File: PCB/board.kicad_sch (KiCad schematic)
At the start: 171 parts, among them J1 Micro_SD_Card, J10 Conn_01x10, J11 Conn_01x02, J12 Conn_02x04_Odd_Even, J13 Conn_01x02, J14 Conn_01x02, J15 Conn_01x03, J16 Conn_01x02, J17 Conn_01x05, J18 Conn_01x04, J19 Conn_01x04, J2 Conn_ARM_JTAG_SWD_10, J20 Conn_01x02, J21 Conn_01x03, J22 Conn_02x04_Odd_Even, J23 Conn_01x04, J24 Conn_01x04, J25 Conn_01x02, J26 Conn_01x03, J27 Conn_02x04_Odd_Even, J28 Conn_01x04, J29 Conn_01x04, J30 Conn_01x02, J31 Conn_01x03, J32 Conn_01x02, J33 Conn_01x02, J34 Conn_01x02, J35 Conn_01x02, J36 Conn_01x02, J37 Conn_01x02, J4 Conn_01x04, J5 Conn_01x04, J6 Conn_01x02, J7 Conn_01x03, J8 Conn_02x04_Odd_Even, J9 Conn_01x10, P1 USB_C_Plug_USB2.0, Q1 IRLML6402, Q2 NMOS, Q3 NMOS, Q4 NMOS, Q5 NMOS, Q6 NMOS, SW1 SW_SPST, SW2 SW_Push, U1 STM32H743VITx, U2 AMS1117-3.3, U3 TPS54331, U4 TMC2209_SILENTSTEPSTICK, U5 TMC2209_SILENTSTEPSTICK, U6 TMC2209_SILENTSTEPSTICK, U7 TMC2209_SILENTSTEPSTICK, Y1 25 MHz

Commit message: added footprints to the PSU
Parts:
- C17: footprint (none) -> Capacitor_THT:CP_Radial_D6.3mm_P2.50mm
- D2: footprint (none) -> Package_TO_SOT_THT:TO-220-2_Horizontal_TabDown
- F1: footprint (none) -> Fuse:Fuse_1812_4532Metric
- J37: footprint (none) -> TerminalBlock_Phoenix:TerminalBlock_Phoenix_MKDS-1,5-2-5.08_1x02_P5.08mm_Horizontal
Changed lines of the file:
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@@
 			)
 		)
-		(property "Footprint" ""
+		(property "Footprint" "Capacitor_THT:CP_Radial_D6.3mm_P2.50mm"
 			(at 83.5152 31.75 0)
 			(effects
@@
 			)
 		)
-		(property "Footprint" ""
+		(property "Footprint" "TerminalBlock_Phoenix:TerminalBlock_Phoenix_MKDS-1,5-2-5.08_1x02_P5.08mm_Horizontal"
 			(at 69.85 26.67 0)
 			(effects
@@
 			)
 		)
-		(property "Footprint" ""
+		(property "Footprint" "Package_TO_SOT_THT:TO-220-2_Horizontal_TabDown"
 			(at 77.47 27.94 0)
 			(effects
@@
 			)
 		)
-		(property "Footprint" ""
+		(property "Footprint" "Fuse:Fuse_1812_4532Metric"
 			(at 87.63 25.908 90)
 			(effects

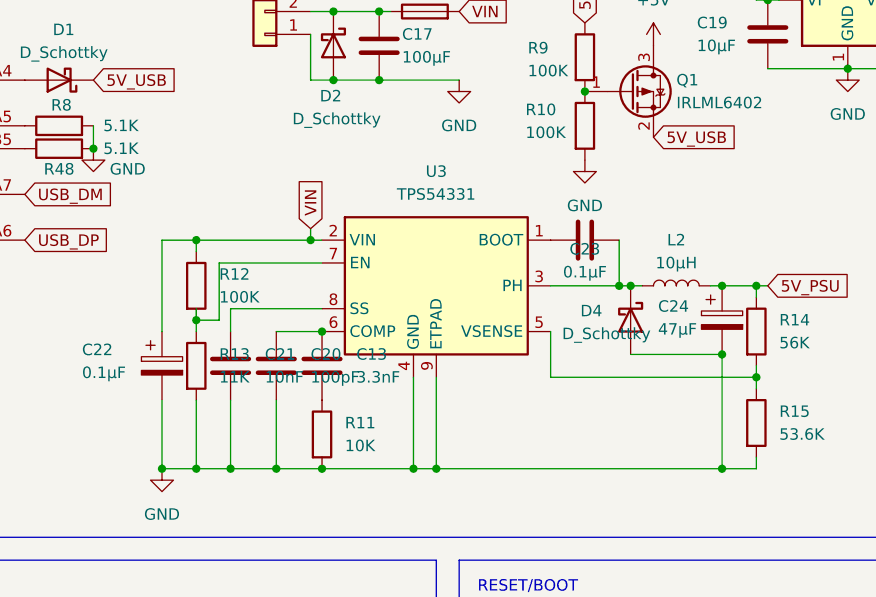
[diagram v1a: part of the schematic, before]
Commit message: footprints for psu
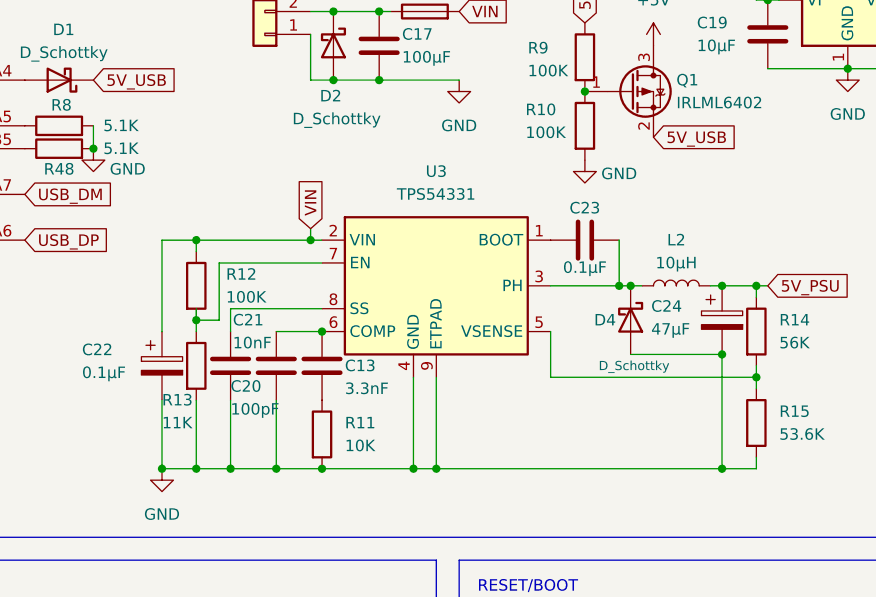
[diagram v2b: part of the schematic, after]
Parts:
- C13, C20, C21, C22, C23: footprint (none) -> Capacitor_SMD:C_0603_1608Metric
- C24: footprint (none) -> Capacitor_SMD:CP_Elec_6.3x5.8
- D4: footprint (none) -> Diode_SMD:D_SMA
- F1: footprint Fuse:Fuse_1812_4532Metric -> Fuse:Fuse_Blade_Mini_directSolder
- L2: footprint (none) -> Inductor_SMD:L_Bourns-SRN8040_8x8.15mm
- R11, R12, R13, R14, R15: footprint (none) -> Resistor_SMD:R_0603_1608Metric
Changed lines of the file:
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@@
 			)
 		)
-		(property "Footprint" ""
+		(property "Footprint" "Resistor_SMD:R_0603_1608Metric"
 			(at 122.682 69.85 90)
 			(effects
@@
 			)
 		)
-		(property "Footprint" ""
+		(property "Footprint" "Resistor_SMD:R_0603_1608Metric"
 			(at 122.682 59.69 90)
 			(effects
@@
 		(on_board yes)
 		(dnp no)
-		(fields_autoplaced yes)
 		(property "Reference" "C13"
-			(at 80.01 62.2299 0)
+			(at 78.74 63.5 0)
 			(effects
 				(font
@@
 		)
 		(property "Value" "3.3nF"
-			(at 80.01 64.7699 0)
+			(at 78.74 66.04 0)
 			(effects
 				(font
@@
 			)
 		)
-		(property "Footprint" ""
+		(property "Footprint" "Capacitor_SMD:C_0603_1608Metric"
 			(at 77.1652 67.31 0)
 			(effects
@@
 			)
 		)
-		(property "Footprint" "Fuse:Fuse_1812_4532Metric"
+		(property "Footprint" "Fuse:Fuse_Blade_Mini_directSolder"
 			(at 87.63 25.908 90)
 			(effects
@@
 			)
 		)
-		(property "Footprint" ""
+		(property "Footprint" "Resistor_SMD:R_0603_1608Metric"
 			(at 74.422 71.12 90)
 			(effects
@@
 		(dnp no)
 		(property "Reference" "C23"
-			(at 105.41 50.546 90)
+			(at 105.41 45.974 90)
 			(effects
 				(font
@@
 		)
 		(property "Value" "0.1µF"
-			(at 105.41 53.086 90)
+			(at 105.41 52.578 90)
 			(effects
 				(font
@@
 			)
 		)
-		(property "Footprint" ""
+		(property "Footprint" "Capacitor_SMD:C_0603_1608Metric"
 			(at 109.22 48.5648 0)
 			(effects
@@
 		(dnp no)
 		(property "Reference" "C24"
-			(at 113.538 56.896 0)
+			(at 112.776 56.896 0)
 			(effects
 				(font
@@
 		)
 		(property "Value" "47µF"
-			(at 113.538 59.436 0)
+			(at 112.776 59.436 0)
 			(effects
 				(font
@@
 			)
 		)
-		(property "Footprint" ""
+		(property "Footprint" "Capacitor_SMD:CP_Elec_6.3x5.8"
 			(at 121.6152 62.23 0)
 			(effects
@@
 		(on_board yes)
 		(dnp no)
-		(fields_autoplaced yes)
 		(property "Reference" "R12"
-			(at 64.77 53.3399 0)
+			(at 65.532 53.34 0)
 			(effects
 				(font
@@
 		)
 		(property "Value" "100K"
-			(at 64.77 55.8799 0)
+			(at 65.532 55.88 0)
 			(effects
 				(font
@@
 			)
 		)
-		(property "Footprint" ""
+		(property "Footprint" "Resistor_SMD:R_0603_1608Metric"
 			(at 60.452 54.61 90)
 			(effects
@@
 			)
 		)
-		(property "Footprint" ""
+		(property "Footprint" "Capacitor_SMD:C_0603_1608Metric"
 			(at 59.3852 67.31 0)
 			(effects
@@
 		(dnp no)
 		(property "Reference" "D4"
-			(at 104.902 57.404 90)
+			(at 106.426 58.42 90)
 			(effects
 				(font
@@
 		)
 		(property "Value" "D_Schottky"
-			(at 102.87 59.944 90)
+			(at 106.934 63.5 90)
 			(effects
 				(font
-					(size 1.27 1.27)
+					(size 1.016 1.016)
 				)
 				(justify left)
 			)
 		)
-		(property "Footprint" ""
+		(property "Footprint" "Diode_SMD:D_SMA"
 			(at 110.49 58.42 0)
 			(effects
@@
 		(on_board yes)
 		(dnp no)
-		(fields_autoplaced yes)
 		(property "Reference" "C21"
-			(at 69.85 62.2299 0)
+			(at 66.294 58.42 0)
 			(effects
 				(font
@@
 		)
 		(property "Value" "10nF"
-			(at 69.85 64.7699 0)
+			(at 66.294 60.96 0)
 			(effects
 				(font
@@
 			)
 		)
-		(property "Footprint" ""
+		(property "Footprint" "Capacitor_SMD:C_0603_1608Metric"
 			(at 67.0052 67.31 0)
 			(effects
@@
 		(dnp no)
 		(property "Reference" "C20"
-			(at 74.93 62.2299 0)
+			(at 66.04 65.786 0)
 			(effects
 				(font
@@
 		)
 		(property "Value" "100pF"
-			(at 74.93 64.7699 0)
+			(at 66.04 68.326 0)
 			(effects
 				(font
@@
 			)
 		)
-		(property "Footprint" ""
+		(property "Footprint" "Capacitor_SMD:C_0603_1608Metric"
 			(at 72.0852 67.31 0)
 			(effects
@@
 		(on_board yes)
 		(dnp no)
-		(fields_autoplaced yes)
 		(property "Reference" "R13"
-			(at 64.77 62.2299 0)
+			(at 58.42 67.31 0)
 			(effects
 				(font
@@
 		)
 		(property "Value" "11K"
-			(at 64.77 64.7699 0)
+			(at 58.42 69.85 0)
 			(effects
 				(font
@@
 			)
 		)
-		(property "Footprint" ""
+		(property "Footprint" "Resistor_SMD:R_0603_1608Metric"
 			(at 60.452 63.5 90)
 			(effects
@@
 		(on_board yes)
 		(dnp no)
-		(fields_autoplaced yes)
 		(property "Reference" "#PWR017"
 			(at 105.41 46.99 0)
@@
 		)
 		(property "Value" "GND"
-			(at 105.41 45.72 0)
+			(at 109.22 42.164 0)
 			(effects
 				(font
@@
 			)
 		)
-		(property "Footprint" ""
+		(property "Footprint" "Inductor_SMD:L_Bourns-SRN8040_8x8.15mm"
 			(at 115.57 54.61 0)
 			(effects

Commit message: finished all the footprints for the power
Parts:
- C18, C19: footprint (none) -> Capacitor_SMD:C_0805_2012Metric
- R10, R9: footprint (none) -> Resistor_SMD:R_0603_1608Metric
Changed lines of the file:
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@@
 			)
 		)
-		(property "Footprint" ""
+		(property "Footprint" "Capacitor_SMD:C_0805_2012Metric"
 			(at 144.4752 30.48 0)
 			(effects
@@
 			)
 		)
-		(property "Footprint" ""
+		(property "Footprint" "Capacitor_SMD:C_0805_2012Metric"
 			(at 126.6952 30.48 0)
 			(effects
@@
 			)
 		)
-		(property "Footprint" ""
+		(property "Footprint" "Resistor_SMD:R_0603_1608Metric"
 			(at 103.632 36.83 90)
 			(effects
@@
 			)
 		)
-		(property "Footprint" ""
+		(property "Footprint" "Resistor_SMD:R_0603_1608Metric"
 			(at 103.632 29.21 90)
 			(effects

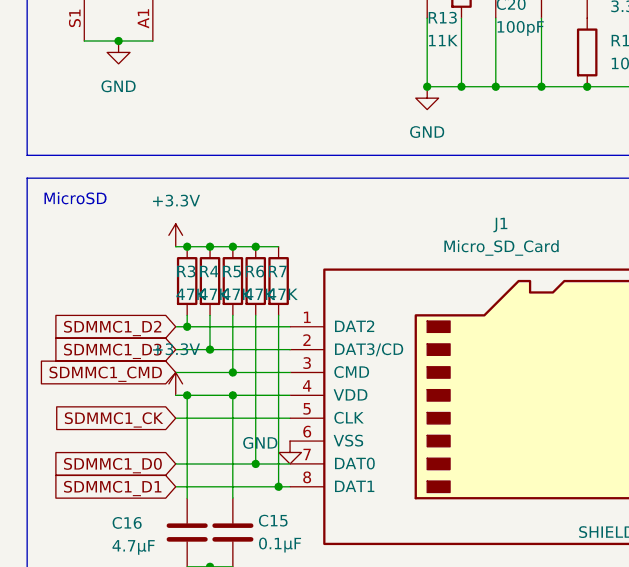
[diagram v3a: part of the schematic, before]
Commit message: sd card footprints
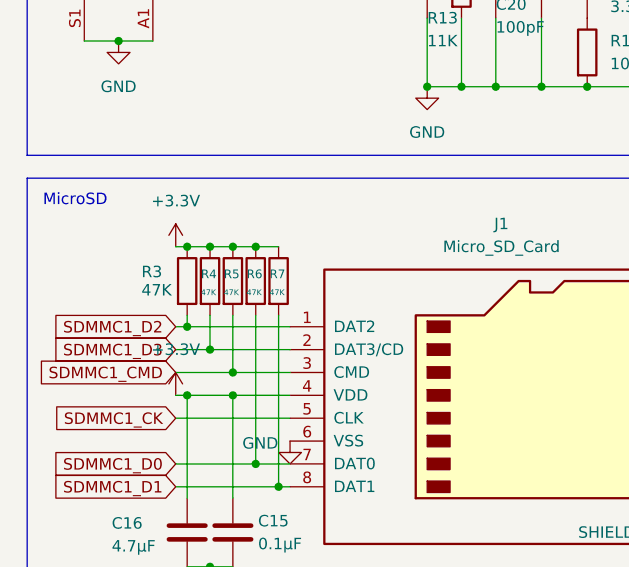
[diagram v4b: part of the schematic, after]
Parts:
- C15: footprint (none) -> Capacitor_SMD:C_0603_1608Metric
- C16: footprint (none) -> Capacitor_SMD:C_0805_2012Metric
- R3, R4, R5, R6, R7: footprint (none) -> Resistor_SMD:R_0603_1608Metric
